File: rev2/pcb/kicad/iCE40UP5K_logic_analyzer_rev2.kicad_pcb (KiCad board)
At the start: 4 copper layers, 89.7 x 82.9 mm, 170 parts, among them IC1 ICE40UP5K-SG48I, IC2 MIC5504-3.3YM5-TR, IC3 MIC5504-1.2YM5-TR, IC4 FT2232HL-TRAY, IC5 W25Q40CLSNIG, IC6 SN74LVC14ADBRE4, IC7 SN74LVC14ADBRE4, IC8 SN74LVC14ADBRE4, J1 USB B Female Connector, J2 61300611121, J3 61202021621, J4 61300821121, J5 61300821121, J6 61300311121, J7 61300621121, Q1 2N7002H6327XTSA2, Y1 830208214809

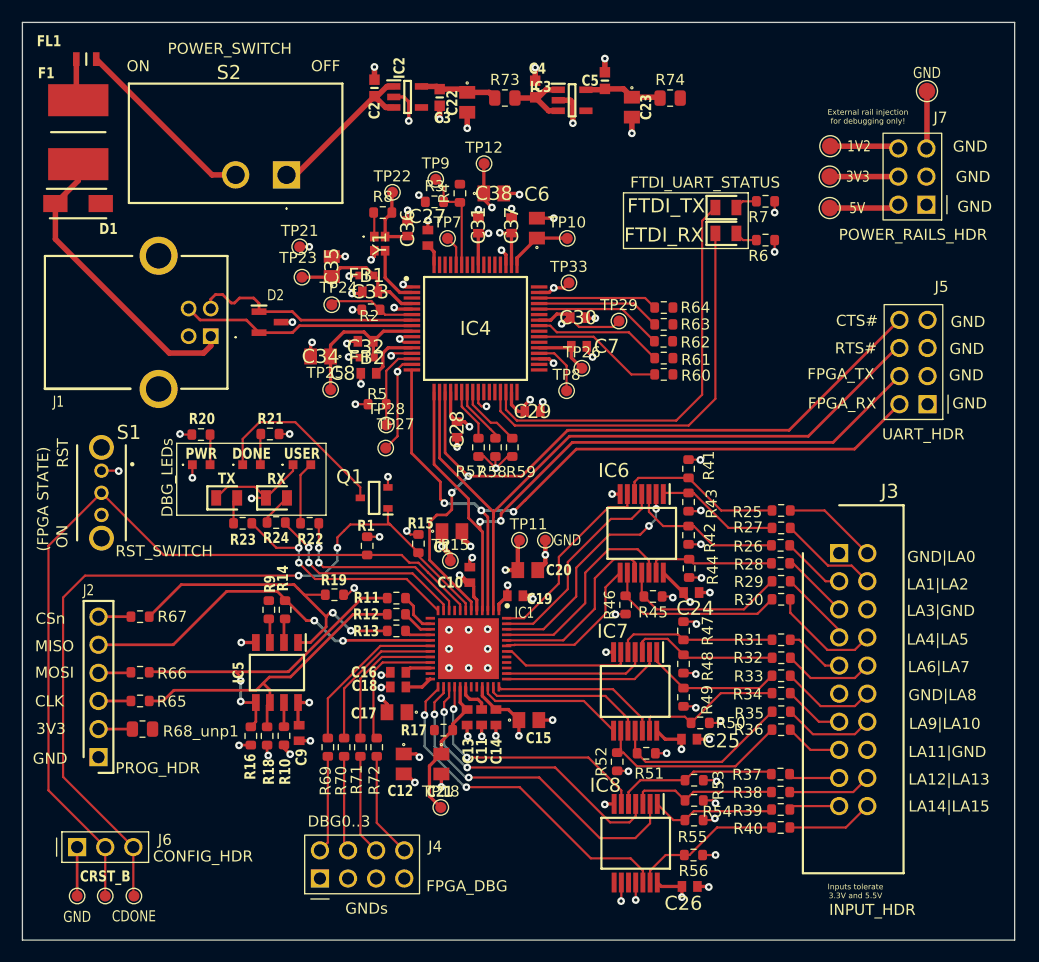
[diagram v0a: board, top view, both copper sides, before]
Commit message: layout sorted with power pours on L3 and silkscreen
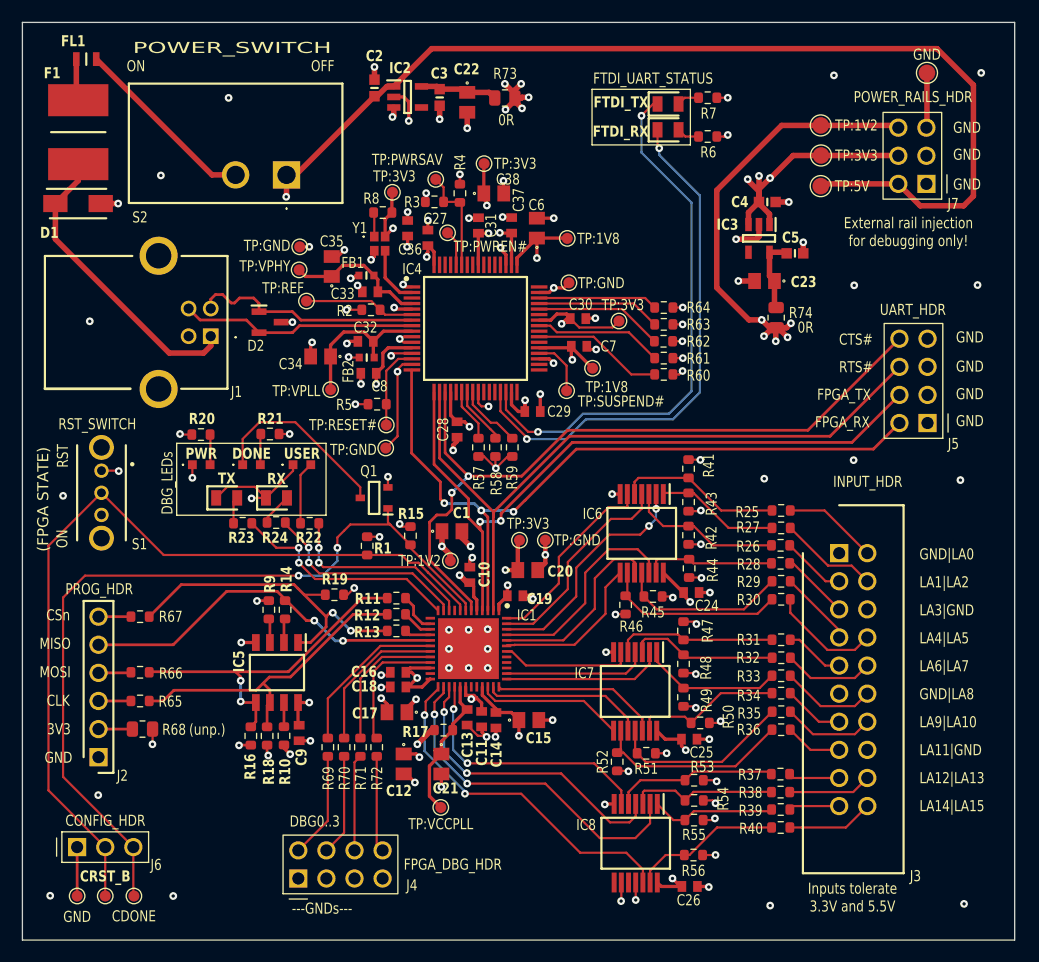
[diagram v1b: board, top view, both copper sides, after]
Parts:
- J4, J5: footprint LIB_2x4_61300821121:J_Wurth_WR-PHD_61300821121 -> 8pin_header_2x4_61300821121:J_Wurth_WR-PHD_61300821121
- J6: footprint LIB_1x3_61300311121:J_Wurth_WR-PHD_61300311121 -> 8pin_header_2x4_61300821121:J_Wurth_WR-PHD_61300311121
- J7: footprint LIB_2x4_61300821121:J_Wurth_WR-PHD_61300621121 -> 6pin_header_2x3_61300621121:J_Wurth_WR-PHD_61300621121
- moved C4 23.3 mm to (198.4, 79.3), turned to 0 degrees
- moved C5 23.2 mm to (200.9, 83.9), turned to 0 degrees
- moved R74 22.0 mm to (199.2, 89.7), turned to -90 degrees
- moved IC3 21.0 mm to (197.6, 82.5), turned to -90 degrees
- moved C23 19.8 mm to (198.1, 86.4), turned to 180 degrees
- moved D8 10.7 mm to (189.4, 72.7)
- moved D9 10.7 mm to (189.4, 70.4)
- moved R6 10.7 mm to (193.0, 73.3)
- moved R7 10.7 mm to (193.0, 69.8)
- moved TP:REF 2.31 mm to (156.7, 88.2)
- moved TP1 2.14 mm to (203.2, 77.8)
- moved TP3 2.07 mm to (203.2, 72.3)
- moved TP2 2.06 mm to (203.2, 75.1)
- moved J4 1.96 mm to (156.0, 140.4)
- moved J7 1.88 mm to (212.8, 77.6)
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- renumbered R68_unp1 to R68, TP15 to TP:1V2, TP26 to TP:1V8, TP10 to TP:1V8, TP12 to TP:3V3, TP29 to TP:3V3, TP11 to TP:3V3, TP22 to TP:3V3, TP21 to TP:GND, TP33 to TP:GND, TP27 to TP:GND, TP7 to TP:PWREN#, TP9 to TP:PWRSAV, TP24 to TP:REF, TP28 to TP:RESET#, TP8 to TP:SUSPEND#, TP18 to TP:VCCPLL, TP23 to TP:VPHY, TP25 to TP:VPLL
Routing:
- net +5V: track 22.6 -> 98.6 mm, vias 1 -> 4
- net +1V2: track 17.3 -> 54.0 mm, vias 3 -> 10
- net +3V3: track 91.9 -> 121.6 mm, vias 24 -> 43
- net /FTDI_TX_LED#: track 38.1 -> 49.4 mm, vias 0 -> 2
- net /FTDI_RX_LED#: track 37.6 -> 47.9 mm, vias 0 -> 2
- net +1V8: track 18.1 -> 23.6 mm, vias 0 -> 4
- net GND: track 134.3 -> 138.3 mm, vias 90 -> 106
- net /FTDI_REF: track 7.89 -> 10.0 mm
- net /FPGA_DBG1: track 8.65 -> 9.67 mm
- net /FPGA_DBG3: track 9.53 -> 8.72 mm
- net /FPGA_DBG0: track 8.80 -> 9.61 mm
- net /FTDI_VPHY: track 12.3 -> 13.0 mm
- net /FPGA_UART_TX: track 66.3 -> 65.6 mm
- net /FPGA_UART_RX: track 68.1 -> 67.3 mm
- net /CTS#: track 69.0 -> 68.3 mm
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- added copper zone on In2.Cu, net +1V2
- added copper zone on In2.Cu, net +1V8
- added copper zone on In2.Cu, net +3V3
- added copper zone on In2.Cu, net +5V
- added copper zone on In2.Cu, net GND
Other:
- board text added: "(unp.)"
- board text added: "---GNDs---"
- board text added: "0R"
- board text added: "FPGA_DBG_HDR"
- board text added: "Logic Analyzer iCE40 UP5K Revision 2 10-07-2026 //JKO"
- board text added: "TP23"
- board text removed: "${REFERENCE}"
- board text removed: "FPGA_DBG"
- board text removed: "GNDs"
- board text removed: "Logic Analyzer iCE40 UP5K Revision 2 26-06-2026 //JKO"
